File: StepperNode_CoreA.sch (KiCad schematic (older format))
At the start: 1 part

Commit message: Setup Node Core Channel B
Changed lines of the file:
@@
 $Descr A3 16535 11693
 encoding utf-8
-Sheet 5 9
+Sheet 5 11
 Title "Stepper Node - Core A"
 Date ""
@@
 	1    0    0    -1
 $EndComp
-Text HLabel 3300 5650 2    60   BiDi ~ 0
+Text HLabel 1450 4900 2    60   BiDi ~ 0
 CHA_I2C_SDA
-Text HLabel 3300 5750 2    60   Output ~ 0
+Text HLabel 1450 5000 2    60   Output ~ 0
 CHA_I2C_SCL
-Text HLabel 3300 4300 2    60   Output ~ 0
+Text HLabel 1450 5300 2    60   Output ~ 0
 CHA_NDSC_CLR_0
-Text HLabel 3300 4400 2    60   Output ~ 0
+Text HLabel 1450 5400 2    60   Output ~ 0
 CHA_NDAC_CLR_1
-Text HLabel 3300 4600 2    60   Output ~ 0
+Text HLabel 1450 5500 2    60   Output ~ 0
 CHA_DAC_NRST
-Text HLabel 3300 4700 2    60   Input ~ 0
+Text HLabel 1450 5600 2    60   Input ~ 0
 CHA_DAC_NDATA_AVAIL
-Text HLabel 3300 4800 2    60   Output ~ 0
+Text HLabel 1450 5700 2    60   Output ~ 0
 CHA_DAC_NCNVT
+Text HLabel 1450 6100 2    60   Output ~ 0
+CHA_STEP1_DIR
+Text HLabel 1450 6200 2    60   Output ~ 0
+CHA_STEP1_STEP
+Text HLabel 1450 6300 2    60   Output ~ 0
+CHA_STEP2_DIR
+Text HLabel 1450 6400 2    60   Output ~ 0
+CHA_STEP2_STEP
+Text HLabel 1450 6500 2    60   Output ~ 0
+CHA_STEP3_DIR
+Text HLabel 1450 6600 2    60   Output ~ 0
+CHA_STEP3_STEP
+Text HLabel 1450 6700 2    60   Output ~ 0
+CHA_STEP4_DIR
+Text HLabel 1450 6800 2    60   Output ~ 0
+CHA_STEP4_STEP
+Text HLabel 1450 6900 2    60   Output ~ 0
+CHA_STEP5_DIR
+Text HLabel 1450 7000 2    60   Output ~ 0
+CHA_STEP5_STEP
+Text HLabel 1450 7100 2    60   Output ~ 0
+CHA_STEP6_DIR
+Text HLabel 1450 7200 2    60   Output ~ 0
+CHA_STEP6_STEP
 $EndSCHEMATC

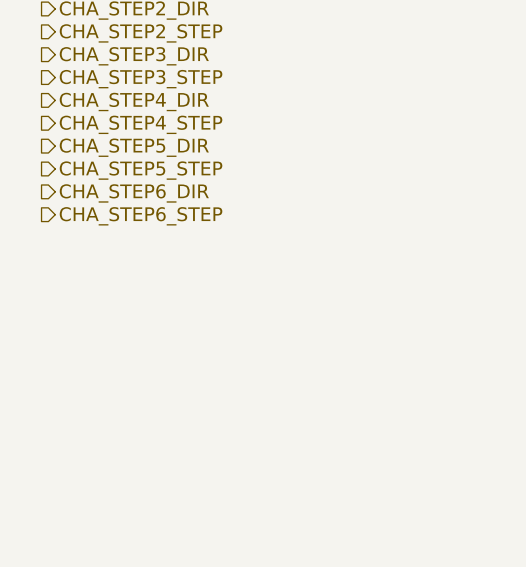
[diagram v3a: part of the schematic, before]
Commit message: Setup Watchdog Sheet
Watchdog is for Channel A/B priority determination.
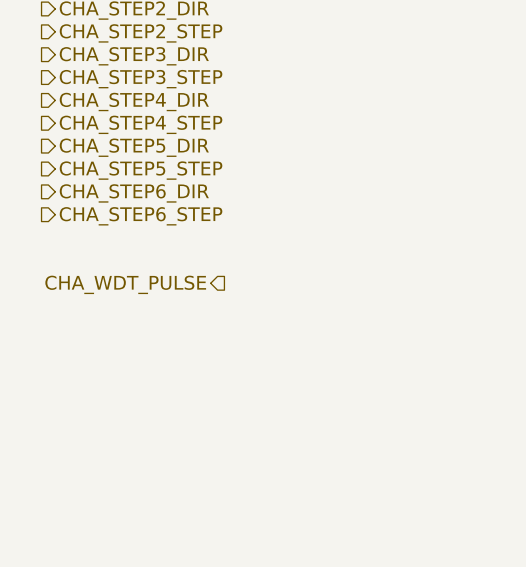
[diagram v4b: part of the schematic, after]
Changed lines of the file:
@@
 $Descr A3 16535 11693
 encoding utf-8
-Sheet 9 12
+Sheet 9 13
 Title "Stepper Node - Core A"
 Date ""
@@
 Text HLabel 1450 7200 2    60   Output ~ 0
 CHA_STEP6_STEP
+Text HLabel 2250 7500 0    60   Output ~ 0
+CHA_WDT_PULSE
 $EndSCHEMATC

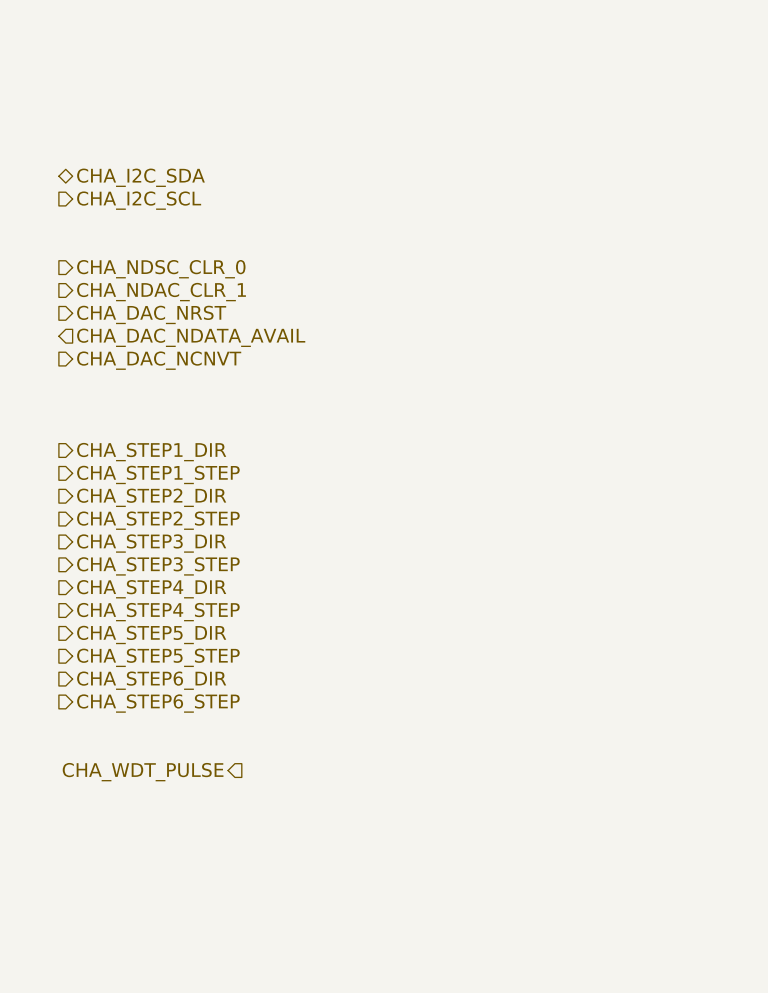
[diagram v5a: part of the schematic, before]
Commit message: Added Aux Prop Interface Sheet
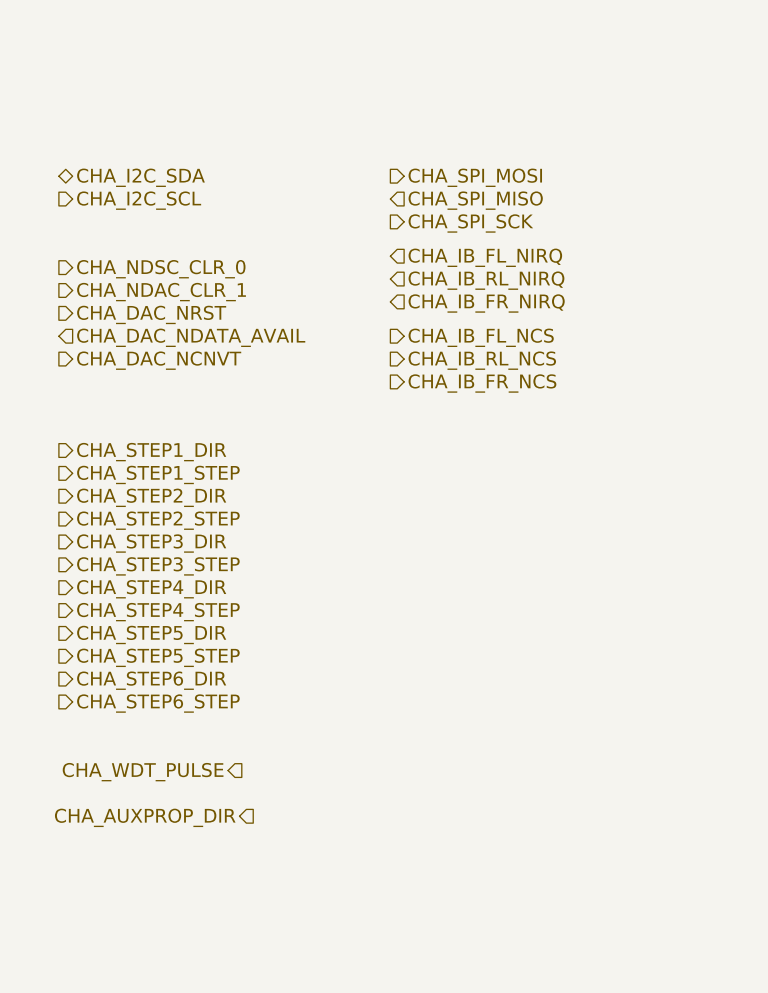
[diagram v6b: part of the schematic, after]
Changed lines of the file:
@@
 $Descr A3 16535 11693
 encoding utf-8
-Sheet 9 14
+Sheet 9 16
 Title "Stepper Node - Core A"
 Date ""
@@
 Text HLabel 2250 7500 0    60   Output ~ 0
 CHA_WDT_PULSE
+Text HLabel 2900 5250 2    60   Input ~ 0
+CHA_IB_FL_NIRQ
+Text HLabel 2900 5350 2    60   Input ~ 0
+CHA_IB_RL_NIRQ
+Text HLabel 2900 5450 2    60   Input ~ 0
+CHA_IB_FR_NIRQ
+Text HLabel 2900 5700 2    60   Output ~ 0
+CHA_IB_RL_NCS
+Text HLabel 2900 5800 2    60   Output ~ 0
+CHA_IB_FR_NCS
+Text HLabel 2900 5600 2    60   Output ~ 0
+CHA_IB_FL_NCS
+Text HLabel 2900 4900 2    60   Output ~ 0
+CHA_SPI_MOSI
+Text HLabel 2900 5000 2    60   Input ~ 0
+CHA_SPI_MISO
+Text HLabel 2900 5100 2    60   Output ~ 0
+CHA_SPI_SCK
+Text HLabel 2300 7700 0    60   Output ~ 0
+CHA_AUXPROP_DIR
 $EndSCHEMATC

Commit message: Netlist top level
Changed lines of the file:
@@
 $Descr A3 16535 11693
 encoding utf-8
-Sheet 9 16
+Sheet 8 16
 Title "Stepper Node - Core A"
 Date ""
@@
 Text HLabel 2300 7700 0    60   Output ~ 0
 CHA_AUXPROP_DIR
+Text HLabel 2150 8000 0    60   Input ~ 0
+PUSH_INTLK_A
+Text HLabel 2150 8100 0    60   Input ~ 0
+PUSH_INTLK_B
+Text HLabel 2900 6150 2    60   Input ~ 0
+CHA_ACCEL1_NINT
+Text HLabel 2900 6250 2    60   Input ~ 0
+CHA_ACCEL2_NINT
 $EndSCHEMATC
